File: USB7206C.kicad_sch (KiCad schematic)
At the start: 33 parts, among them J1 USB_SPI_(Opt), SW1 RESET_HUB, U1 USB7206C/KDX, U2 MIC803-29D4VM3-TR, Y1 25MHz

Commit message: labels naming fixes, USB Type E connector added
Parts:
- removed R1: 10k, symbol Device:R
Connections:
- net VBUS_DET: now reaches U1.2 (PF30/VBUS_MON_UP)
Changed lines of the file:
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@@
 	(wire
 		(pts
-			(xy 38.1 29.21) (xy 55.88 29.21)
+			(xy 266.7 262.89) (xy 276.86 262.89)
 		)
 		(stroke
@@
 	(wire
 		(pts
-			(xy 266.7 262.89) (xy 276.86 262.89)
+			(xy 39.37 74.93) (xy 55.88 74.93)
 		)
 		(stroke
@@
 	(wire
 		(pts
-			(xy 39.37 74.93) (xy 55.88 74.93)
+			(xy 276.86 254) (xy 280.67 254)
 		)
 		(stroke
@@
 	(wire
 		(pts
-			(xy 276.86 254) (xy 280.67 254)
+			(xy 308.61 40.64) (xy 317.5 40.64)
 		)
 		(stroke
@@
 		)
 	)
-	(wire
+	(bus
 		(pts
-			(xy 308.61 40.64) (xy 317.5 40.64)
+			(xy 194.31 142.24) (xy 194.31 147.32)
 		)
 		(stroke
@@
 		)
 	)
-	(bus
+	(wire
 		(pts
-			(xy 194.31 142.24) (xy 194.31 147.32)
+			(xy 43.18 27.94) (xy 43.18 29.21)
 		)
 		(stroke
@@
 	(wire
 		(pts
+			(xy 43.18 29.21) (xy 55.88 29.21)
+		)
+		(stroke
+			(width 0)
+			(type default)
+		)
+	)
+	(wire
+		(pts
 			(xy 205.74 157.48) (xy 205.74 162.56)
 		)
@@
 		)
 	)
-	(hierarchical_label "USB_DN2{USB3}"
+	(hierarchical_label "USB_DN2"
 		(shape output)
 		(at 13.97 57.15 180)
@@
 		)
 	)
+	(hierarchical_label "VBUS_DET"
+		(shape input)
+		(at 43.18 27.94 180)
+		(effects
+			(font
+				(size 1.27 1.27)
+			)
+			(justify right)
+		)
+	)
 	(symbol
 		(lib_id "2025-07-15_10-11-24:USB7206C_KDX")
@@
 	)
 	(symbol
-		(lib_id "Device:R")
-		(at 38.1 25.4 0)
-		(unit 1)
-		(exclude_from_sim no)
-		(in_bom yes)
-		(on_board yes)
-		(dnp no)
-		(fields_autoplaced yes)
-		(property "Reference" "R1"
-			(at 40.64 24.1299 0)
-			(effects
-				(font
-					(size 1.27 1.27)
-				)
-				(justify left)
-			)
-		)
-		(property "Value" "10k"
-			(at 40.64 26.6699 0)
-			(effects
-				(font
-					(size 1.27 1.27)
-				)
-				(justify left)
-			)
-		)
-		(property "Footprint" ""
-			(at 36.322 25.4 90)
-			(effects
-				(font
-					(size 1.27 1.27)
-				)
-				(hide yes)
-			)
-		)
-		(property "Datasheet" "~"
-			(at 38.1 25.4 0)
-			(effects
-				(font
-					(size 1.27 1.27)
-				)
-				(hide yes)
-			)
-		)
-		(property "Description" "Resistor"
-			(at 38.1 25.4 0)
-			(effects
-				(font
-					(size 1.27 1.27)
-				)
-				(hide yes)
-			)
-		)
-		(pin "2"
-		)
-		(pin "1"
-		)
-		(instances
-			(project ""
-				(path "/a2586c28-95f1-49e6-9254-37d7a8473e53/84084c93-70ae-4353-a3b8-87defd735fb2"
-					(reference "R1")
-					(unit 1)
-				)
-			)
-		)
-	)
-	(symbol
 		(lib_id "power:GND")
 		(at 198.12 264.16 0)
@@
 					(unit 1)
 				)
-			)
-		)
-	)
-	(symbol
-		(lib_id "power:+3V3")
-		(at 38.1 21.59 0)
-		(unit 1)
-		(exclude_from_sim no)
-		(in_bom yes)
-		(on_board yes)
-		(dnp no)
-		(fields_autoplaced yes)
-		(property "Reference" "#PWR02"
-			(at 38.1 25.4 0)
-			(effects
-				(font
-					(size 1.27 1.27)
-				)
-				(hide yes)
-			)
-		)
-		(property "Value" "+3V3"
-			(at 38.1 16.51 0)
-			(effects
-				(font
-					(size 1.27 1.27)
-				)
-			)
-		)
-		(property "Footprint" ""
-			(at 38.1 21.59 0)
-			(effects
-				(font
-					(size 1.27 1.27)
-				)
-				(hide yes)
-			)
-		)
-		(property "Datasheet" ""
-			(at 38.1 21.59 0)
-			(effects
-				(font
-					(size 1.27 1.27)
-				)
-				(hide yes)
-			)
-		)
-		(property "Description" "Power symbol creates a global label with name \"+3V3\""
-			(at 38.1 21.59 0)
-			(effects
-				(font
-					(size 1.27 1.27)
-				)
-				(hide yes)
-			)
-		)
-		(pin "1"
-		)
-		(instances
-			(project "USB_hub"
-				(path "/a2586c28-95f1-49e6-9254-37d7a8473e53/84084c93-70ae-4353-a3b8-87defd735fb2"
-					(reference "#PWR02")
-					(unit 1)
-				)

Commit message: Port Power Control added to USB7206C schematics
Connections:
- net PRT_CTL4: now reaches U1.57 (PF14)
- net PRT_CTL3: now reaches U1.58 (PF15)
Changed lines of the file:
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@@
+	(wire
+		(pts
+			(xy 31.75 137.16) (xy 53.34 137.16)
+		)
+		(stroke
+			(width 0)
+			(type default)
+		)
+	)
 	(wire
 		(pts
@@
 		(pts
 			(xy 257.81 267.97) (xy 252.73 267.97)
+		)
+		(stroke
+			(width 0)
+			(type default)
+		)
+	)
+	(wire
+		(pts
+			(xy 31.75 134.62) (xy 53.34 134.62)
 		)
 		(stroke
@@
 		)
 	)
+	(hierarchical_label "PRT_CTL4"
+		(shape output)
+		(at 31.75 134.62 180)
+		(effects
+			(font
+				(size 1.27 1.27)
+			)
+			(justify right)
+		)
+	)
 	(hierarchical_label "USB_UP"
 		(shape input)
@@
 		(effects
 			(font
+				(size 1.27 1.27)
+			)
+			(justify right)
+		)
+	)
+	(hierarchical_label "PRT_CTL3"
+		(shape output)
+		(at 31.75 137.16 180)
+		(effects
+			(font

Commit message: TPS25762 EEPROM connector added
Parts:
- renumbered R2 to R1, R3 to R2, R4 to R3, R5 to R4, R6 to R5, R7 to R6
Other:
- title: (none) -> USB Hub

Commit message: deleted duplicated capacitor
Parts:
- C1, C10, C11, C12, C13, C14, C15, C16, C17, C18, C19, C2, C20, C21, C3, C4, C5, C6, C7, C8, C9: footprint (none) -> Capacitor_SMD:C_0402_1005Metric
- J1: footprint (none) -> Connector_PinHeader_1.27mm:PinHeader_1x05_P1.27mm_Vertical
- R1, R2, R3, R4, R5, R6: footprint (none) -> Resistor_SMD:R_0603_1608Metric
- SW1: footprint (none) -> Button_Switch_SMD:SW_Push_1P1T_XKB_TS-1187A
- U1: footprint VQFN100_KDX_MCH -> Package_QFP:VQFP-100_14x14mm_P0.5mm
- Y1: footprint (none) -> Crystal:Crystal_SMD_0603-4Pin_6.0x3.5mm
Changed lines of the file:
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@@
 			)
 		)
-		(property "Footprint" "VQFN100_KDX_MCH"
+		(property "Footprint" "Package_QFP:VQFP-100_14x14mm_P0.5mm"
 			(at 55.88 26.67 0)
 			(effects
@@
 			)
 		)
-		(property "Footprint" ""
+		(property "Footprint" "Capacitor_SMD:C_0402_1005Metric"
 			(at 318.4652 48.26 0)
 			(effects
@@
 			)
 		)
-		(property "Footprint" ""
+		(property "Footprint" "Capacitor_SMD:C_0402_1005Metric"
 			(at 173.0248 256.54 0)
 			(effects
@@
 			)
 		)
-		(property "Footprint" ""
+		(property "Footprint" "Resistor_SMD:R_0603_1608Metric"
 			(at 254.762 259.08 90)
 			(effects
@@
 			)
 		)
-		(property "Footprint" ""
+		(property "Footprint" "Capacitor_SMD:C_0402_1005Metric"
 			(at 351.4852 27.94 0)
 			(effects
@@
 			)
 		)
-		(property "Footprint" ""
+		(property "Footprint" "Capacitor_SMD:C_0402_1005Metric"
 			(at 268.9352 48.26 0)
 			(effects
@@
 			)
 		)
-		(property "Footprint" ""
+		(property "Footprint" "Capacitor_SMD:C_0402_1005Metric"
 			(at 252.4252 48.26 0)
 			(effects
@@
 			)
 		)
-		(property "Footprint" ""
+		(property "Footprint" "Resistor_SMD:R_0603_1608Metric"
 			(at 44.45 156.718 90)
 			(effects
@@
 			)
 		)
-		(property "Footprint" ""
+		(property "Footprint" "Capacitor_SMD:C_0402_1005Metric"
 			(at 334.9752 27.94 0)
 			(effects
@@
 			)
 		)
-		(property "Footprint" ""
+		(property "Footprint" "Capacitor_SMD:C_0402_1005Metric"
 			(at 268.9352 27.94 0)
 			(effects
@@
 			)
 		)
-		(property "Footprint" ""
+		(property "Footprint" "Capacitor_SMD:C_0402_1005Metric"
 			(at 197.1548 256.54 0)
 			(effects
@@
 			)
 		)
-		(property "Footprint" ""
+		(property "Footprint" "Connector_PinHeader_1.27mm:PinHeader_1x05_P1.27mm_Vertical"
 			(at 19.05 167.64 0)
 			(effects
@@
 			)
 		)
-		(property "Footprint" "VQFN100_KDX_MCH"
+		(property "Footprint" "Package_QFP:VQFP-100_14x14mm_P0.5mm"
 			(at 53.34 121.92 0)
 			(effects
@@
 			)
 		)
-		(property "Footprint" ""
+		(property "Footprint" "Capacitor_SMD:C_0402_1005Metric"
 			(at 367.9952 27.94 0)
 			(effects
@@
 			)
 		)
-		(property "Footprint" ""
+		(property "Footprint" "Capacitor_SMD:C_0402_1005Metric"
 			(at 375.6152 27.94 0)
 			(effects
@@
 			)
 		)
-		(property "Footprint" ""
+		(property "Footprint" "Capacitor_SMD:C_0402_1005Metric"
 			(at 351.4852 48.26 0)
 			(effects
@@
 			)
 		)
-		(property "Footprint" ""
+		(property "Footprint" "Button_Switch_SMD:SW_Push_1P1T_XKB_TS-1187A"
 			(at 271.78 248.92 0)
 			(effects
@@
 			)
 		)
-		(property "Footprint" ""
+		(property "Footprint" "Capacitor_SMD:C_0402_1005Metric"
 			(at 301.9552 27.94 0)
 			(effects
@@
 			)
 		)
-		(property "Footprint" ""
+		(property "Footprint" "Capacitor_SMD:C_0402_1005Metric"
 			(at 318.4652 27.94 0)
 			(effects
@@
 			)
 		)
-		(property "Footprint" ""
+		(property "Footprint" "Capacitor_SMD:C_0402_1005Metric"
 			(at 285.4452 48.26 0)
 			(effects
@@
 			)
 		)
-		(property "Footprint" ""
+		(property "Footprint" "Resistor_SMD:R_0603_1608Metric"
 			(at 50.8 265.938 90)
 			(effects
@@
 			)
 		)
-		(property "Footprint" ""
+		(property "Footprint" "Capacitor_SMD:C_0402_1005Metric"
 			(at 301.9552 48.26 0)
 			(effects
@@
 			)
 		)
-		(property "Footprint" ""
+		(property "Footprint" "Resistor_SMD:R_0603_1608Metric"
 			(at 204.47 126.238 90)
 			(effects
@@
 			)
 		)
-		(property "Footprint" ""
+		(property "Footprint" "Capacitor_SMD:C_0402_1005Metric"
 			(at 235.9152 27.94 0)
 			(effects
@@
 			)
 		)
-		(property "Footprint" ""
+		(property "Footprint" "Capacitor_SMD:C_0402_1005Metric"
 			(at 334.9752 48.26 0)
 			(effects
@@
 			)
 		)
-		(property "Footprint" ""
+		(property "Footprint" "Crystal:Crystal_SMD_0603-4Pin_6.0x3.5mm"
 			(at 186.69 255.27 0)
 			(effects
@@
 			)
 		)
-		(property "Footprint" ""
+		(property "Footprint" "Resistor_SMD:R_0603_1608Metric"
 			(at 44.45 151.638 90)
 			(effects
@@
 			)
 		)
-		(property "Footprint" ""
+		(property "Footprint" "Capacitor_SMD:C_0402_1005Metric"
 			(at 359.1052 48.26 0)
 			(effects
@@
 			)
 		)
-		(property "Footprint" ""
+		(property "Footprint" "Resistor_SMD:R_0603_1608Metric"
 			(at 44.45 154.178 90)
 			(effects
@@
 			)
 		)
-		(property "Footprint" ""
+		(property "Footprint" "Capacitor_SMD:C_0402_1005Metric"
 			(at 252.4252 27.94 0)
 			(effects
@@
 			)
 		)
-		(property "Footprint" ""
+		(property "Footprint" "Capacitor_SMD:C_0402_1005Metric"
 			(at 235.9152 48.26 0)
 			(effects
@@
 			)
 		)
-		(property "Footprint" ""
+		(property "Footprint" "Capacitor_SMD:C_0402_1005Metric"
 			(at 285.4452 27.94 0)
 			(effects

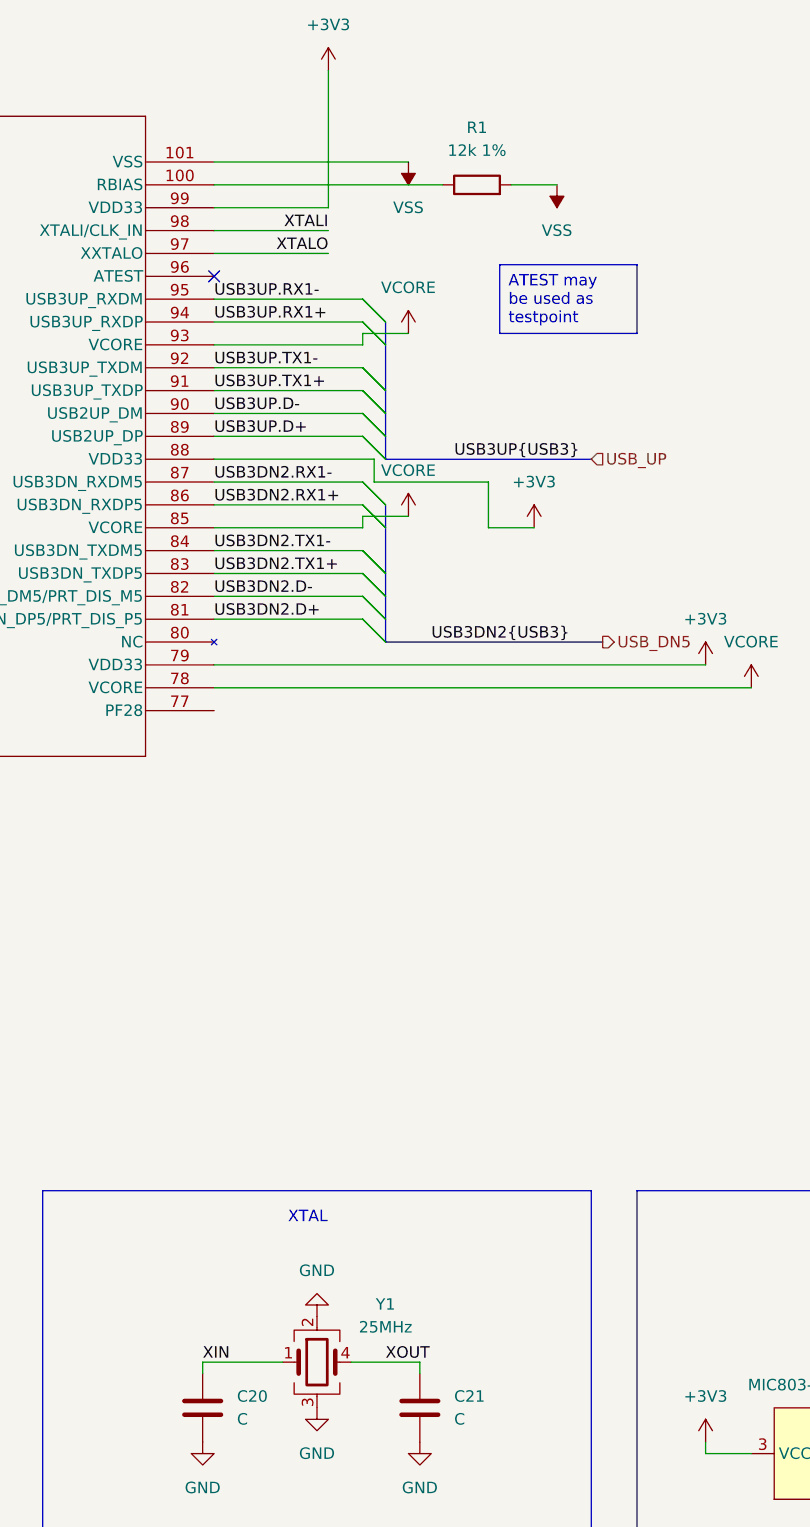
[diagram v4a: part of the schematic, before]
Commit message: Minor fixes
Fixed unclear labelling of buses
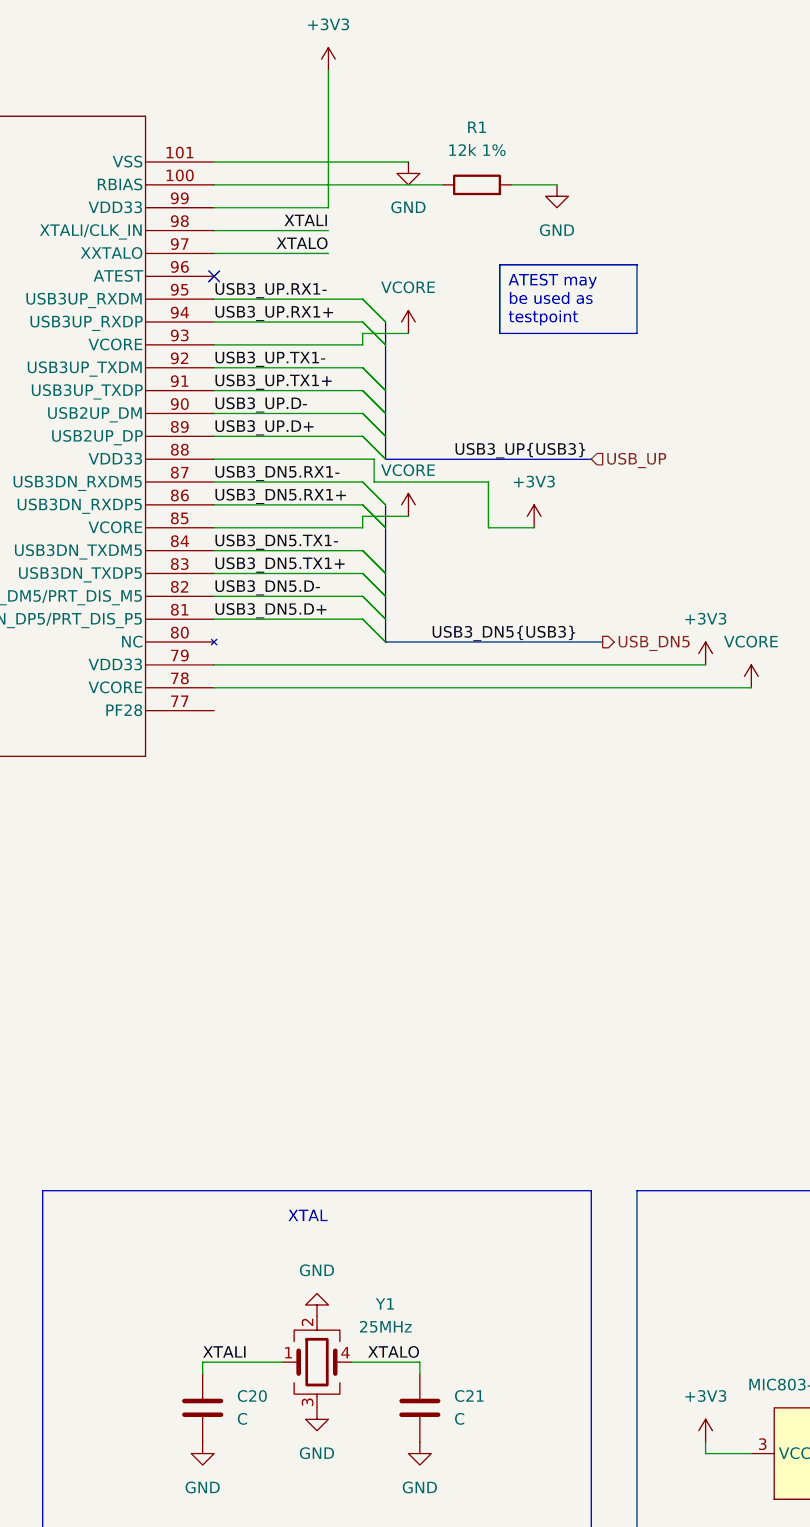
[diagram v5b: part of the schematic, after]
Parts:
- R1, R2, R3, R4, R5, R6: footprint Resistor_SMD:R_0603_1608Metric -> Resistor_SMD:R_0402_1005Metric
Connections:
- net VSS is gone; now on net GND: R1.2, U1.101 (VSS)
- net XIN is gone; now on net XTALI: C20.2, Y1.1
- net XOUT is gone; now on net XTALO: C21.2, Y1.4
- net USB3DN2.D+ renamed USB3_DN5.D+
- net USB3DN2.D- renamed USB3_DN5.D-
- net USB3DN2.RX1+ renamed USB3_DN5.RX1+
- net USB3DN2.RX1- renamed USB3_DN5.RX1-
- net USB3DN2.TX1+ renamed USB3_DN5.TX1+
- net USB3DN2.TX1- renamed USB3_DN5.TX1-
- net USB3UP.D+ renamed USB3_UP.D+
- net USB3UP.D- renamed USB3_UP.D-
- net USB3UP.RX1+ renamed USB3_UP.RX1+
- net USB3UP.RX1- renamed USB3_UP.RX1-
- net USB3UP.TX1+ renamed USB3_UP.TX1+
- net USB3UP.TX1- renamed USB3_UP.TX1-
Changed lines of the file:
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@@
 		)
 	)
-	(label "USB3UP.D+"
+	(label "USB3_UP.D+"
 		(at 175.26 152.4 0)
 		(effects
@@
 		)
 	)
-	(label "USB3DN2.TX1-"
+	(label "USB3_DN5.TX1-"
 		(at 175.26 165.1 0)
 		(effects
@@
 		)
 	)
-	(label "USB3UP.RX1-"
+	(label "USB3_UP.RX1-"
 		(at 175.26 137.16 0)
 		(effects
@@
 		)
 	)
-	(label "USB3UP.RX1+"
+	(label "USB3_UP.RX1+"
 		(at 175.26 139.7 0)
 		(effects
@@
 		)
 	)
-	(label "XIN"
-		(at 173.99 255.27 0)
-		(effects
-			(font
-				(size 1.27 1.27)
-			)
-			(justify left bottom)
-		)
-	)
 	(label "CFG_STRAP2"
 		(at 30.48 261.62 0)
@@
 		)
 	)
-	(label "USB3DN2.TX1+"
+	(label "USB3_DN5.TX1+"
 		(at 175.26 167.64 0)
 		(effects
@@
 		)
 	)
-	(label "USB3DN2.D-"
+	(label "USB3_DN5.D-"
 		(at 175.26 170.18 0)
 		(effects
@@
 		)
 	)
+	(label "XTALO"
+		(at 198.12 255.27 180)
+		(effects
+			(font
+				(size 1.27 1.27)
+			)
+			(justify right bottom)
+		)
+	)
 	(label "USB3_DN3.TX1+"
 		(at 167.64 82.55 0)
@@
 		)
 	)
+	(label "XTALI"
+		(at 173.99 255.27 0)
+		(effects
+			(font
+				(size 1.27 1.27)
+			)
+			(justify left bottom)
+		)
+	)
 	(label "SMBus_MSTR.SDA"
 		(at 34.29 31.75 0)
@@
 		)
 	)
-	(label "USB3UP.TX1-"
+	(label "USB3_UP.TX1-"
 		(at 175.26 144.78 0)
 		(effects
@@
 		)
 	)
-	(label "USB3DN2.RX1-"
+	(label "USB3_DN5.RX1-"
 		(at 175.26 157.48 0)
 		(effects
@@
 		)
 	)
-	(label "XOUT"
-		(at 194.31 255.27 0)
-		(effects
-			(font
-				(size 1.27 1.27)
-			)
-			(justify left bottom)
-		)
-	)
 	(label "CFG_BC_EN"
 		(at 40.64 167.64 0)
@@
 		)
 	)
-	(label "USB3UP.D-"
+	(label "USB3_UP.D-"
 		(at 175.26 149.86 0)
 		(effects
@@
 		)
 	)
-	(label "USB3DN2.D+"
+	(label "USB3_DN5.D+"
 		(at 175.26 172.72 0)
 		(effects
@@
 		)
 	)
-	(label "USB3UP{USB3}"
+	(label "USB3_UP{USB3}"
 		(at 201.93 154.94 0)
 		(effects
@@
 		)
 	)
-	(label "USB3UP.TX1+"
+	(label "USB3_UP.TX1+"
 		(at 175.26 147.32 0)
 		(effects
@@
 		)
 	)
-	(label "USB3DN2.RX1+"
+	(label "USB3_DN5.RX1+"
 		(at 175.26 160.02 0)
 		(effects
@@
 		)
 	)
-	(label "USB3DN2{USB3}"
+	(label "USB3_DN5{USB3}"
 		(at 199.39 175.26 0)
 		(effects
@@
 			)
 		)
-		(property "Footprint" "Resistor_SMD:R_0603_1608Metric"
+		(property "Footprint" "Resistor_SMD:R_0402_1005Metric"
 			(at 254.762 259.08 90)
 			(effects
@@
 			)
 		)
-		(property "Footprint" "Resistor_SMD:R_0603_1608Metric"
+		(property "Footprint" "Resistor_SMD:R_0402_1005Metric"
 			(at 44.45 156.718 90)
 			(effects
@@
 	)
 	(symbol
-		(lib_id "power:VSS")
-		(at 213.36 124.46 180)
-		(unit 1)
-		(exclude_from_sim no)
-		(in_bom yes)
-		(on_board yes)
-		(dnp no)
-		(fields_autoplaced yes)
-		(property "Reference" "#PWR016"
-			(at 213.36 120.65 0)
-			(effects
-				(font
-					(size 1.27 1.27)
-				)
-				(hide yes)
-			)
-		)
-		(property "Value" "VSS"
-			(at 213.36 129.54 0)
-			(effects
-				(font
-					(size 1.27 1.27)
-				)
-			)
-		)
-		(property "Footprint" ""
-			(at 213.36 124.46 0)
-			(effects
-				(font
-					(size 1.27 1.27)
-				)
-				(hide yes)
-			)
-		)
-		(property "Datasheet" ""
-			(at 213.36 124.46 0)
-			(effects
-				(font
-					(size 1.27 1.27)
-				)
-				(hide yes)
-			)
-		)
-		(property "Description" "Power symbol creates a global label with name \"VSS\""
-			(at 213.36 124.46 0)
-			(effects
-				(font
-					(size 1.27 1.27)
-				)
-				(hide yes)
-			)
-		)
-		(pin "1"
-		)
-		(instances
-			(project "USB_hub"
-				(path "/a2586c28-95f1-49e6-9254-37d7a8473e53/84084c93-70ae-4353-a3b8-87defd735fb2"
-					(reference "#PWR016")
-					(unit 1)
-				)
-			)
-		)
-	)
-	(symbol
 		(lib_id "power:+3V3")
 		(at 229.87 264.16 0)
@@
 			)
 		)
-		(property "Footprint" "Resistor_SMD:R_0603_1608Metric"
+		(property "Footprint" "Resistor_SMD:R_0402_1005Metric"
 			(at 50.8 265.938 90)
 			(effects
@@
 			)
 		)
-		(property "Footprint" "Resistor_SMD:R_0603_1608Metric"
+		(property "Footprint" "Resistor_SMD:R_0402_1005Metric"
 			(at 204.47 126.238 90)
 			(effects
@@
 	)
 	(symbol
+		(lib_id "power:GND")
+		(at 213.36 124.46 0)
+		(unit 1)
+		(exclude_from_sim no)
+		(in_bom yes)
+		(on_board yes)
+		(dnp no)
+		(fields_autoplaced yes)
+		(property "Reference" "#PWR014"
+			(at 213.36 130.81 0)
+			(effects
+				(font
+					(size 1.27 1.27)
+				)
+				(hide yes)
+			)
+		)
+		(property "Value" "GND"
+			(at 213.36 129.54 0)
+			(effects
+				(font
+					(size 1.27 1.27)
+				)
+			)
+		)
+		(property "Footprint" ""
+			(at 213.36 124.46 0)
+			(effects
+				(font
+					(size 1.27 1.27)
+				)
+				(hide yes)
+			)
+		)
+		(property "Datasheet" ""
+			(at 213.36 124.46 0)
+			(effects
+				(font
+					(size 1.27 1.27)
+				)
+				(hide yes)
+			)
+		)
+		(property "Description" "Power symbol creates a global label with name \"GND\" , ground"
+			(at 213.36 124.46 0)
+			(effects
+				(font
+					(size 1.27 1.27)
+				)
+				(hide yes)
+			)
+		)
+		(pin "1"
+		)
+		(instances
+			(project ""
+				(path "/a2586c28-95f1-49e6-9254-37d7a8473e53/84084c93-70ae-4353-a3b8-87defd735fb2"
+					(reference "#PWR014")
+					(unit 1)
+				)
+			)
+		)
+	)
+	(symbol
 		(lib_id "power:VCC")
 		(at 196.85 140.97 0)
@@
 			)
 		)
-		(property "Footprint" "Resistor_SMD:R_0603_1608Metric"
+		(property "Footprint" "Resistor_SMD:R_0402_1005Metric"
 			(at 44.45 151.638 90)
 			(effects
@@
 	)
 	(symbol
-		(lib_id "power:VSS")
-		(at 196.85 121.92 180)
+		(lib_id "power:GND")
+		(at 196.85 121.92 0)
 		(unit 1)
 		(exclude_from_sim no)
@@
 		(dnp no)
 		(fields_autoplaced yes)
-		(property "Reference" "#PWR014"
-			(at 196.85 118.11 0)
+		(property "Reference" "#PWR016"
+			(at 196.85 128.27 0)
 			(effects
 				(font
@@
 			)
 		)
-		(property "Value" "VSS"
+		(property "Value" "GND"
 			(at 196.85 127 0)
 			(effects
@@
 			)
 		)
-		(property "Description" "Power symbol creates a global label with name \"VSS\""
+		(property "Description" "Power symbol creates a global label with name \"GND\" , ground"
 			(at 196.85 121.92 0)
 			(effects
@@
 			(project ""
 				(path "/a2586c28-95f1-49e6-9254-37d7a8473e53/84084c93-70ae-4353-a3b8-87defd735fb2"
-					(reference "#PWR014")
+					(reference "#PWR016")
 					(unit 1)
 				)
@@
 			)
 		)
-		(property "Footprint" "Resistor_SMD:R_0603_1608Metric"
+		(property "Footprint" "Resistor_SMD:R_0402_1005Metric"
 			(at 44.45 154.178 90)
 			(effects
